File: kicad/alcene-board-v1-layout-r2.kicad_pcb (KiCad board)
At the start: 2 copper layers, 120 x 90 mm, 14 parts, among them J1 ESP32-S3-DevKitC-1_J1, J2 USB-C Input, J3 ESP32-S3-DevKitC-1_J3, J4 ILI9341_TFT_14pin, J5 Male Pin Header 1x18 - J1 Sig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, J6 Male Pin Header 1x18 - J3 Sig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, J7 Male Pin Header 2x4 - GND, J8 Male Pin Header 2x4 - 3V3, J9 Male Pin Header 2x4 - VIN 5V, SW1 ESP32-S3 Reset (NO momentary)

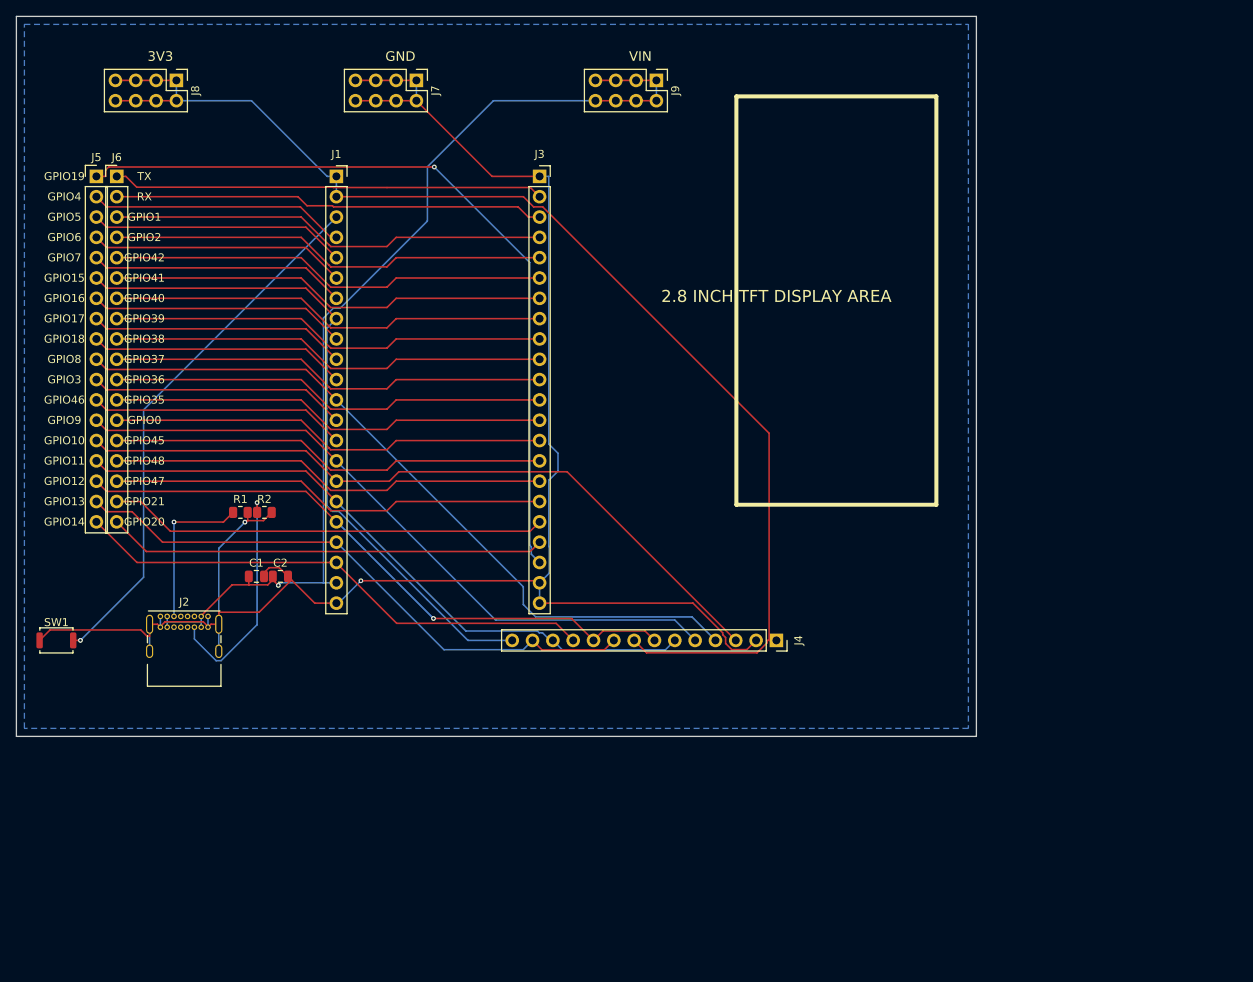
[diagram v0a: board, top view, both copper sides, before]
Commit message: chore: commit all local changes
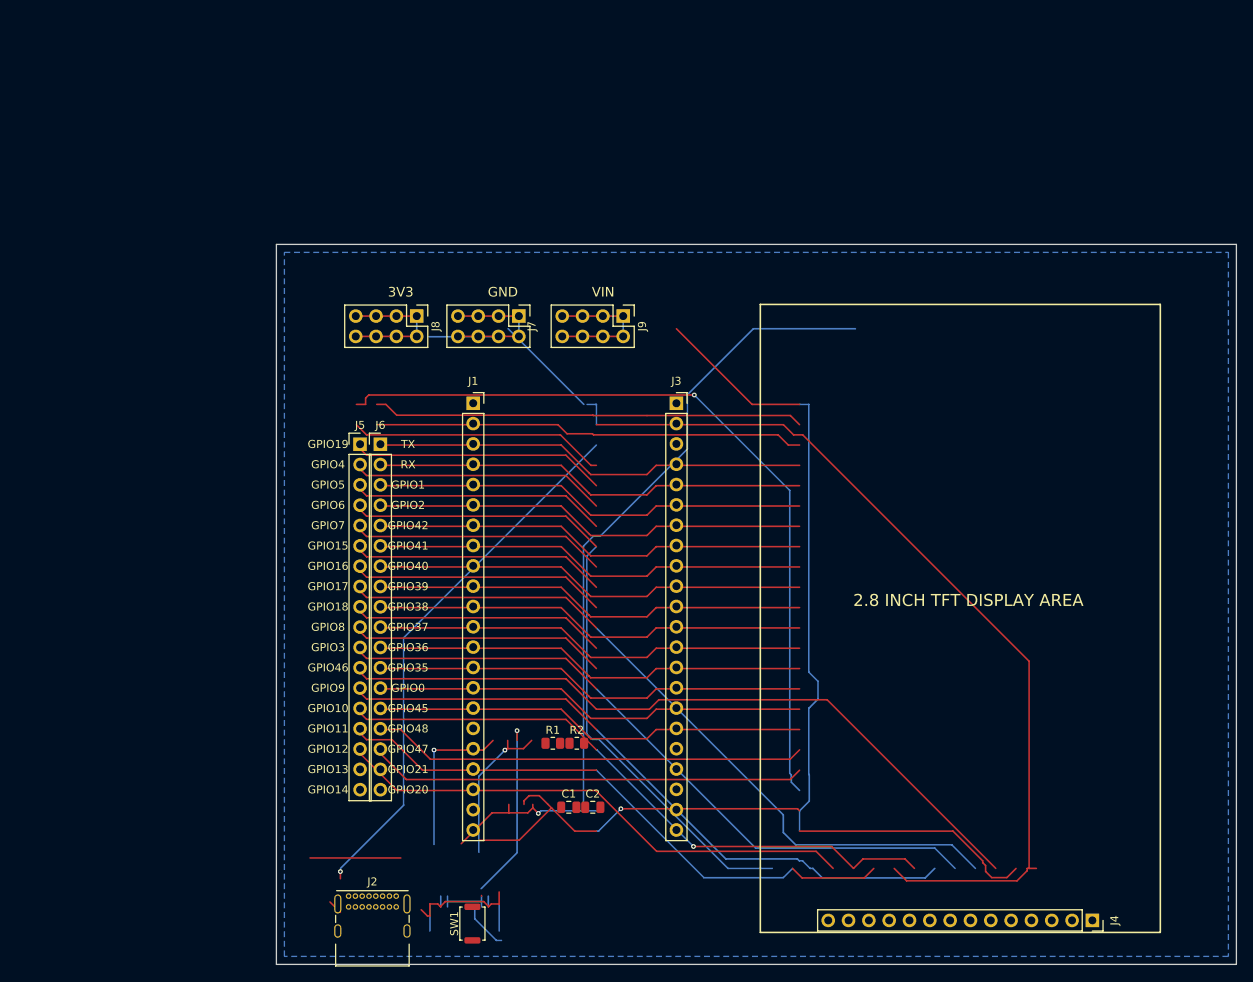
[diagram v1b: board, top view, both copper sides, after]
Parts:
- moved SW1 62.9 mm to (57.0, 113.4), turned to 90 degrees
- moved J4 52.8 mm to (134.5, 113.0)
- moved C1 48.6 mm to (69.0, 98.9)
- moved C2 48.6 mm to (72.0, 98.9)
- moved R1 48.6 mm to (67.0, 90.9)
- moved R2 48.6 mm to (70.0, 90.9)
- moved J5 47.0 mm to (43.0, 53.5)
- moved J6 47.0 mm to (45.5, 53.5)
- moved J2 42.1 mm to (41.5, 110.0)
- moved J8 42.1 mm to (50.0, 37.5)
- moved J1 33.1 mm to (57.1, 48.4)
- moved J3 33.1 mm to (82.5, 48.4)
- moved J7 32.1 mm to (62.8, 37.5)
- moved J9 29.8 mm to (75.8, 37.5)
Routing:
- net GND: track 228.3 -> 402.4 mm, vias 2 -> 3
- net TX: track 53.9 -> 165.4 mm
- net GPIO10: track 91.2 -> 0.00 mm
- net GPIO11: track 82.6 -> 0.00 mm
- net 3V3: track 155.7 -> 75.4 mm
- net GPIO46: track 32.1 -> 91.2 mm
- net GPIO47: track 54.9 -> 109.7 mm
- net GPIO21: track 54.9 -> 0.00 mm
- net GPIO48: track 54.9 -> 109.7 mm
- net GPIO9: track 86.2 -> 32.1 mm
- net GPIO15: track 86.1 -> 32.1 mm
- net RX: track 53.9 -> 0.00 mm
- net GPIO4: track 32.1 -> 64.2 mm
- net GPIO19: track 98.1 -> 130.2 mm
- net GPIO12: track 79.0 -> 51.8 mm
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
